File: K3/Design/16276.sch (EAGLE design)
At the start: 75 parts, among them J1 PST1,0/4-3,5, J3 PBC03SAA, Q1 K1N, Q10 DMB, Q11 34N, Q12 34N, Q13 K1N, Q14 K1N, Q15 K1N, Q16 K38, Q17 K38, Q18 DMB, Q19 K3N, Q2 DMB, Q20 K3N, Q21 K1N, Q22 DMB, Q23 34N, Q24 K84, Q3 34N, Q4 DMB, Q5 K3N, Q6 K1N, Q7 K1N, Q8 K1N, Q9 K1N, U1 MC34063A, U2 74HC238

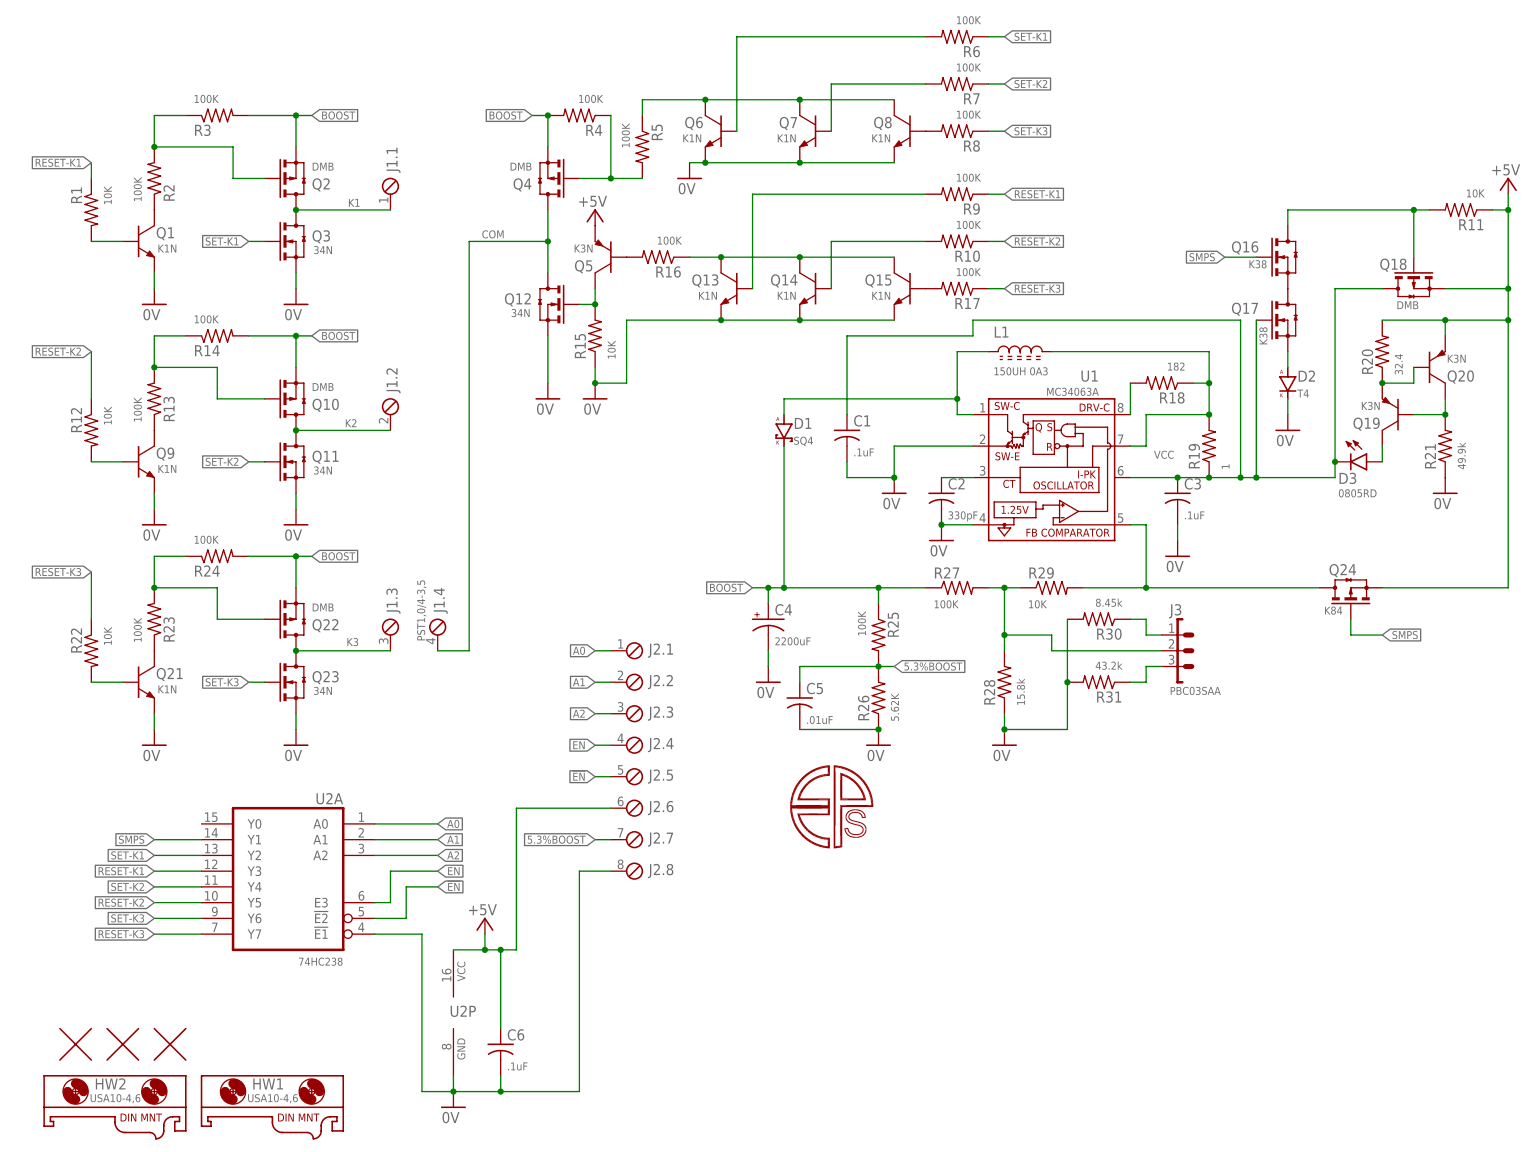
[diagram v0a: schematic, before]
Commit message: K3: use E3 input to turn on curr source
that test for bridge shorts
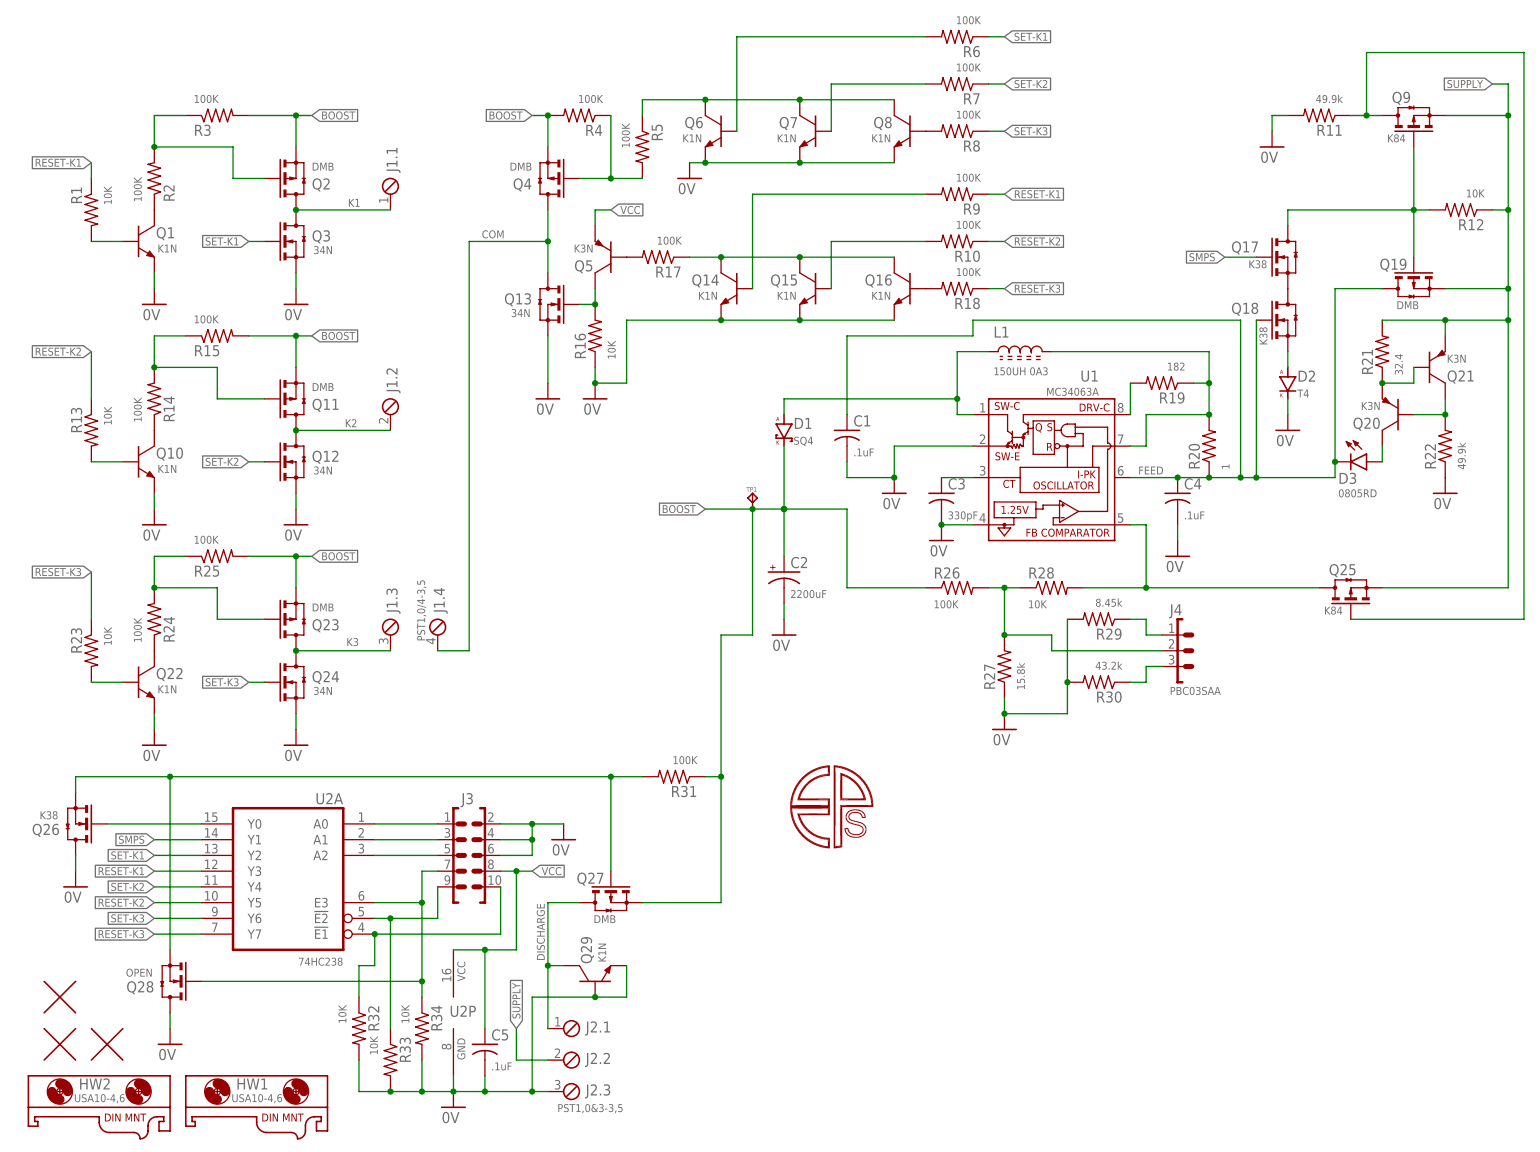
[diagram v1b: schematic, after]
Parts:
- removed C6: .1uF, C-C:CC0603A
- added J4: PBC03SAA, J-HDR2.54mm:1X3
- added Q25: K84, Q-PCH:N-CHSOT23
- added Q26: K38, Q-NCH:N-CHSOT23
- added Q27: DMB, Q-PCH:N-CHSOT23
- added Q28: OPEN, Q-NCH:N-CHSOT23
- added Q29: K1N, Q-NPN:NPNSOT23
- added R32, R33, R34: 10K, R-C:R0805
- added TP1: TPPAD1-08, J-TP:TPPAD1-08
- C2: value 330pF -> 2200uF; device C-C:CC0603A -> C-Al:C-AL7.5X18
- C3: value .1uF -> 330pF
- C4: value 2200uF -> .1uF; device C-Al:C-AL7.5X18 -> C-C:CC0603A
- C5: value .01uF -> .1uF
- J2: value (none) -> PST1,0&3-3,5; device J-HDR3.5mm:MCV8 -> J-HDR3.5mm:MCV3
- J3: value PBC03SAA -> (none); device J-HDR2.54mm:1X3 -> J-HDR2.54mm:2X5
- Q10, Q22: value DMB -> K1N; device Q-PCH:N-CHSOT23 -> Q-NPN:NPNSOT23
- Q11, Q23: value 34N -> DMB; device Q-NCH:N-CHSOT23 -> Q-PCH:N-CHSOT23
- Q13: value K1N -> 34N; device Q-NPN:NPNSOT23 -> Q-NCH:N-CHSOT23
- Q16: value K38 -> K1N; device Q-NCH:N-CHSOT23 -> Q-NPN:NPNSOT23
- Q18: value DMB -> K38; device Q-PCH:N-CHSOT23 -> Q-NCH:N-CHSOT23
- Q19: value K3N -> DMB; device Q-PNP:PNPSOT23 -> Q-PCH:N-CHSOT23
- Q21: value K1N -> K3N; device Q-NPN:NPNSOT23 -> Q-PNP:PNPSOT23
- Q24: value K84 -> 34N; device Q-PCH:N-CHSOT23 -> Q-NCH:N-CHSOT23
- Q9: value K1N -> K84; device Q-NPN:NPNSOT23 -> Q-PCH:N-CHSOT23
- R11, R22: value 10K -> 49.9k
- R13, R16, R23: value 100K -> 10K
- R15: value 10K -> 100K
- R18: value 182 -> 100K
- R19: value 1 -> 182; device R-C:R1210 -> R-C:R0805
- R20: value 32.4 -> 1; device R-C:R0805 -> R-C:R1210
- R21: value 49.9k -> 32.4
- R26: value 5.62K -> 100K
- R27: value 100K -> 15.8k
- R28: value 15.8k -> 10K
- R29: value 10K -> 8.45k
- R30: value 8.45k -> 43.2k
- R31: value 43.2k -> 100K
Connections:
- removed net !EN: J2.5.1, U2A.!E2
- removed net +5V: C6.1, J2.6.1, Q18.S, Q20.E, Q24.S, Q5.E, R11.1, R20.2, U2P.VCC
- removed net 5.3%BOOST: C5.1, J2.7.1, R25.2, R26.2
- removed net EN: J2.4.1, U2A.E3
- new net !E1: J3.10, R32.1, U2A.!E1
- new net !E2: J3.9, R33.1, U2A.!E2
- new net DISCHARGE: J2.1.1, Q27.D, Q29.C
- new net E3: J3.7, Q28.G, R34.1, U2A.E3
- new net FEED: C1.1, C4.1, D3.K, Q18.G, Q19.D, R20.1, U1.VCC
- new net N$10: Q26.S, Q27.G, Q28.S, R31.2
- new net N$11: Q26.G, U2A.Y0
- new net N$2: Q25.G, Q9.D, R11.1
- new net SUPPLY: J2.2.1, Q19.S, Q21.E, Q25.S, Q9.S, R12.1, R21.2
- net 0V: now also C2.-, C4.2, J2.3.1, J3.2, J3.4, J3.6, Q10.E, Q13.S, Q16.E, Q22.E, Q24.S, Q26.D, Q28.D, Q29.B, Q29.E, R11.2, R16.1, R22.1, R27.1, R29.2, R32.2, R33.2, R34.2; no longer C2.2, C4.-, C6.2, J2.8.1, Q11.S, Q13.E, Q21.E, Q23.S, Q9.E, R15.1, R21.1, R26.1, R28.1, R31.2, U2A.!E1
- net A0: now also J3.1; no longer J2.1.1
- net A1: now also J3.3; no longer J2.2.1
- net A2: now also J3.5; no longer J2.3.1
- net BOOST: now also C2.+, Q11.S, Q23.S, Q27.S, R15.2, R25.2, R26.1, R31.1, TP1.TP; no longer C4.+, Q10.S, Q22.S, R14.2, R24.2, R25.1, R27.1
- net COM: now also Q13.D; no longer Q12.D
- net K2: now also Q12.D; no longer Q10.D
- net K3: now also Q24.D; no longer Q22.D
- net N$120: now also J4.3, R30.1; no longer J3.3, R31.1
- net N$121: now also J4.1, R29.1; no longer J3.1, R30.1
- net N$128: now also Q20.E, Q21.B, R21.1; no longer Q19.E, Q20.B, R20.1
- net N$13: now also R19.2; no longer R18.2
- net N$132: now also Q20.B, Q21.C, R22.2; no longer Q19.B, Q20.C, R21.2
- net N$14: now also R19.1, R20.2; no longer R18.1, R19.2
- net N$16: now also C3.1; no longer C2.1
- net N$21: now also Q13.G, R16.2; no longer Q12.G, R15.2
- net N$22: now also Q17.D, Q19.G, Q9.G, R12.2; no longer Q16.D, Q18.G, R11.2
- net N$26: now also J4.2, R26.2, R28.1; no longer J3.2, R28.2, R29.1
- net N$3: now also Q23.G, R24.2, R25.1; no longer Q22.G, R23.2, R24.1
- net N$4: now also Q22.C, R24.1; no longer Q21.C, R23.1
- net N$43: now also Q11.G, R14.2, R15.1; no longer Q10.G, R13.2, R14.1
- net N$44: now also Q10.C, R14.1; no longer Q9.C, R13.1
- net N$45: now also Q10.B, R13.2; no longer Q9.B, R12.2
- net N$5: now also Q22.B, R23.2; no longer Q21.B, R22.2
- net N$6: now also Q17.S, Q18.D; no longer Q16.S, Q17.D
- net N$7: now also Q25.D, R28.2; no longer Q24.D, R29.2
- net N$72: now also R17.2; no longer R16.2
- net N$73: now also Q16.C, R17.1; no longer Q13.C, R16.1
- net N$79: now also Q14.B; no longer Q13.B
- net N$8: now also Q18.S; no longer Q17.S
- net N$81: now also Q15.B; no longer Q14.B
- net N$86: now also Q20.C; no longer Q19.C
- net N$87: now also Q16.B, R18.2; no longer Q15.B, R17.2
- net RESET-K2: now also R13.1; no longer R12.1
- net RESET-K3: now also R18.1, R23.1; no longer R17.1, R22.1
- net SET-K2: now also Q12.G; no longer Q11.G
- net SET-K3: now also Q24.G; no longer Q23.G
- net SMPS: now also Q17.G; no longer Q16.G, Q24.G
- net VCC: now also C5.1, J3.8, Q5.E, U2P.VCC; no longer C1.1, C3.1, D3.K, Q17.G, Q18.D, R19.1, U1.VCC
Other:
- note added: "11/1/16"
- note added: "A0 A1 A2 E3 !E2! !E1! : DESC X X X 0V X X : ALL DISABLED X X X X 5V X : ALL DISABLED X X X X X 5V : ALL DISABLED 0V 0V 0V 5V 0V 0V : DISCHARGE [5V 0V 0V 5V 0V 0V : /W Q27] 5V 0V 0V 5V 0V 0V : BOOST 0V 5V 0V 5V 0V 0V : SET K1 5V 5V 0V 5V 0V 0V : RESET K1 0V 0V 5V 5V 0V 0V : SET K2 5V 0V 5V 5V 0V 0V : RESET K2 0V 5V 5V 5V 0V 0V : SET K3 5V 5V 5V 5V 0V 0V : RESET K3"
- note added: "ESD CLAMP"
- note added: "SHDWN HACK MOD, 2.54MM HDR, Y0 IS CHRG OUTPUT"
- note added: "SHUTDOWN WHILE Q19 OPEN (HI-Z)"
- note added: "[CONNECT BOOST TO PLUGABLE PIN]"
- note added: "[K38]"
- note added: "^1"
- note removed: "10/2/16"
- note removed: "A0 A1 A2 EN !EN! : DESC X X X 0V X : ALL DISABLED X X X X 5V : ALL DISABLED 0V 0V 0V 5V 0V : NC 5V 0V 0V 5V 0V : BOOST 0V 5V 0V 5V 0V : SET K1 5V 5V 0V 5V 0V : RESET K1 0V 0V 5V 5V 0V : SET K2 5V 0V 5V 5V 0V : RESET K2 0V 5V 5V 5V 0V : SET K3 5V 5V 5V 5V 0V : RESET K3"
- moved on the sheet: C3, C5, HW1, HW2, J2.1, J2.2, J2.3, Q11, Q12, Q14, Q15, Q17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

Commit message: K3: ^2 review
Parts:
- removed Q27: DMB, Q-PCH:N-CHSOT23
- removed Q28: OPEN, Q-NCH:N-CHSOT23
- removed Q29: K1N, Q-NPN:NPNSOT23
- R31: value 100K -> JMP
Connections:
- removed net DISCHARGE: J2.1.1, Q27.D, Q29.C
- removed net N$10: Q26.S, Q27.G, Q28.S, R31.2
- removed net N$11: Q26.G, U2A.Y0
- new net EN17MA: Q26.D, R22.1
- net 0V: now also Q26.S; no longer Q26.D, Q28.D, Q29.B, Q29.E, R22.1
- net BOOST: now also J2.1.1, R31.2; no longer Q27.S, TP1.TP
- net E3: now also Q26.G; no longer Q28.G
- net FEED: now also TP1.TP
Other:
- note added: "2/5/17"
- note added: "A0 A1 A2 E3 !E2! !E1! : DESC X X X 0V X X : ALL DISABLED X X X X 5V X : ALL DISABLED X X X X X 5V : ALL DISABLED X X X 5V X X : ENABLE 17mA 5V 0V 0V 5V 0V 0V : BOOST 0V 5V 0V 5V 0V 0V : SET K1 5V 5V 0V 5V 0V 0V : RESET K1 0V 0V 5V 5V 0V 0V : SET K2 5V 0V 5V 5V 0V 0V : RESET K2 0V 5V 5V 5V 0V 0V : SET K3 5V 5V 5V 5V 0V 0V : RESET K3"
- note added: "ENABLE CURR SOURCE NMOS S-D FLIP, RM DISCH"
- note added: "Q19 ONLY ALLOWS POWER TO FLOW WHEN BOOST IS NOT SHORTED WITH 17MA TEST"
- note added: "SHUTDOWN WHILE Q19 IS OFF (HI-Z)"
- note added: "^2"
- note removed: "A0 A1 A2 E3 !E2! !E1! : DESC X X X 0V X X : ALL DISABLED X X X X 5V X : ALL DISABLED X X X X X 5V : ALL DISABLED 0V 0V 0V 5V 0V 0V : DISCHARGE [5V 0V 0V 5V 0V 0V : /W Q27] 5V 0V 0V 5V 0V 0V : BOOST 0V 5V 0V 5V 0V 0V : SET K1 5V 5V 0V 5V 0V 0V : RESET K1 0V 0V 5V 5V 0V 0V : SET K2 5V 0V 5V 5V 0V 0V : RESET K2 0V 5V 5V 5V 0V 0V : SET K3 5V 5V 5V 5V 0V 0V : RESET K3"
- note removed: "ESD CLAMP"
- note removed: "PMOS ONLY ALLOWS POWER TO FLOW WHEN BOOST IS NOT SHORTED WITH 20MA TEST"
- note removed: "SHUTDOWN WHILE Q19 OPEN (HI-Z)"
- note removed: "[CONNECT BOOST TO PLUGABLE PIN]"
- note removed: "[K38]"
- moved on the sheet: Q20, Q21, Q26, R21, R22, R31, TP1
